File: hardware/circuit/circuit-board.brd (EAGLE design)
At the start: 20 x 73.7 mm, 14 parts, among them U1 ADUM1200CRZ

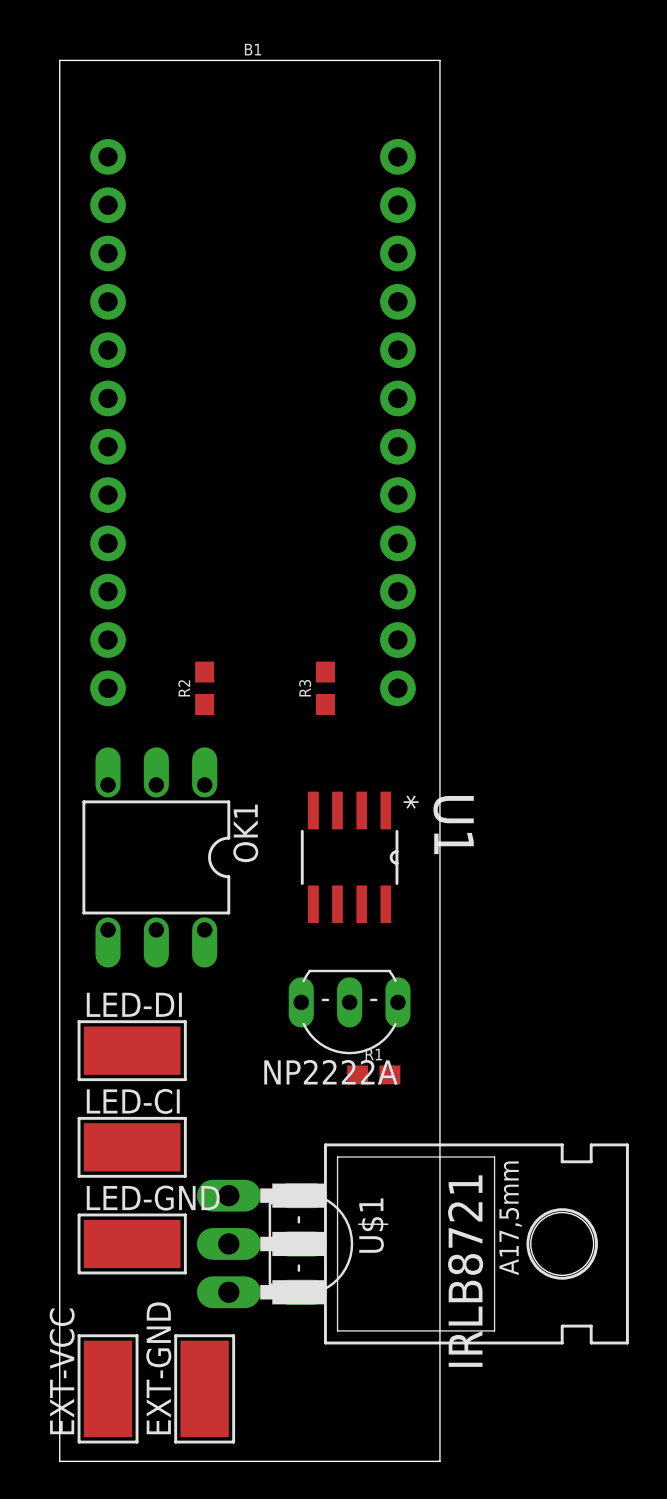
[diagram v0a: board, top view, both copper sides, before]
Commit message: Added autorouted routes, thickened GND-A (LED ground thru MOSFET) traces, this will probably do, will run through DRUs and send it out tomorrow
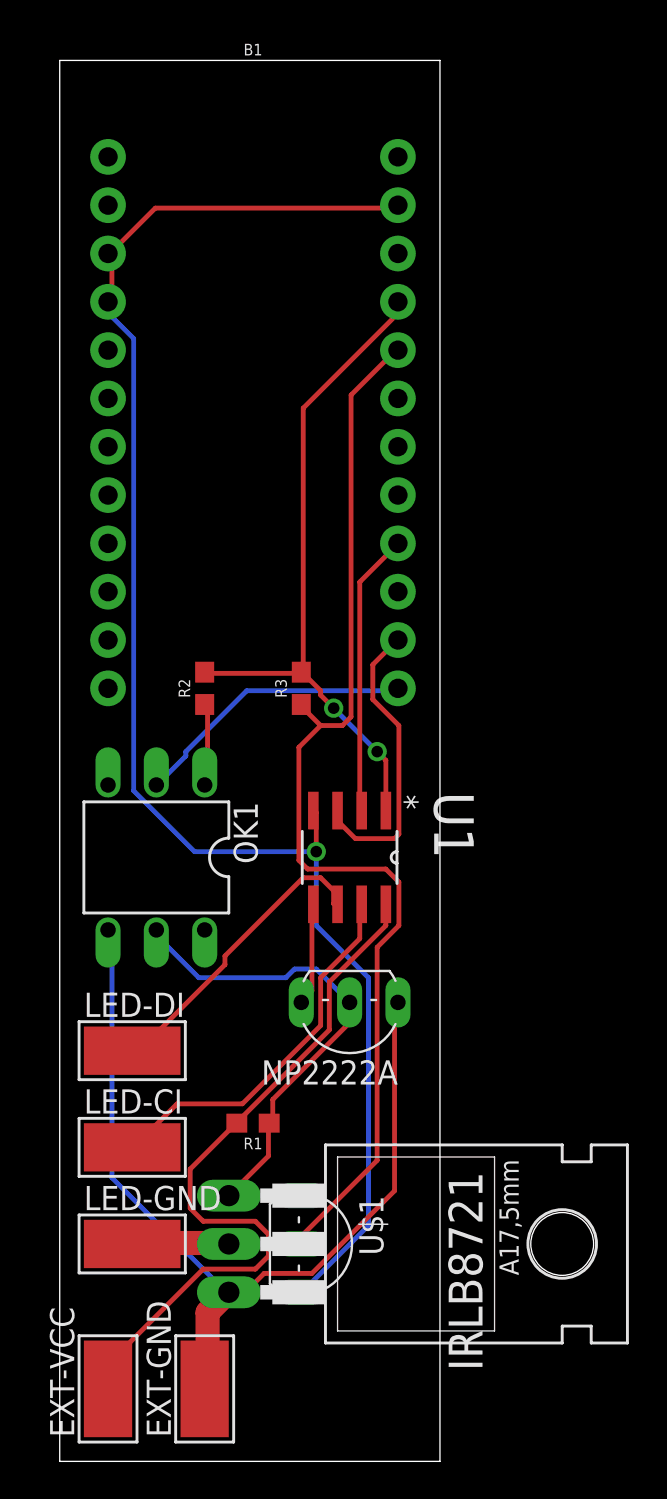
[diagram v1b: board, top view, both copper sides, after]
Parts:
- moved R1 6.84 mm to (10.2, 24.1), turned to 180 degrees
- moved R3 1.27 mm to (12.7, 47.0)
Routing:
- net GND: track 0.00 -> 84.3 mm, vias 0 -> 1
- net TEMP: track 0.00 -> 58.1 mm
- net GNDA: track 0.00 -> 48.5 mm
- net +5V: track 0.00 -> 38.2 mm
- net VCC: track 0.00 -> 35.8 mm, vias 0 -> 2
- net PWR-CTRL: track 0.00 -> 25.2 mm
- net N$7: track 0.00 -> 19.8 mm
- net N$1: track 0.00 -> 15.8 mm
- net N$5: track 0.00 -> 15.6 mm
- net N$8: track 0.00 -> 14.9 mm
- net N$6: track 0.00 -> 14.9 mm
- net ADUM-GND2: track 0.00 -> 5.39 mm
- net N$3: track 0.00 -> 5.10 mm
- net N$4: track 0.00 -> 4.35 mm

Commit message: Added to PCB layout - added ground layers, some labels
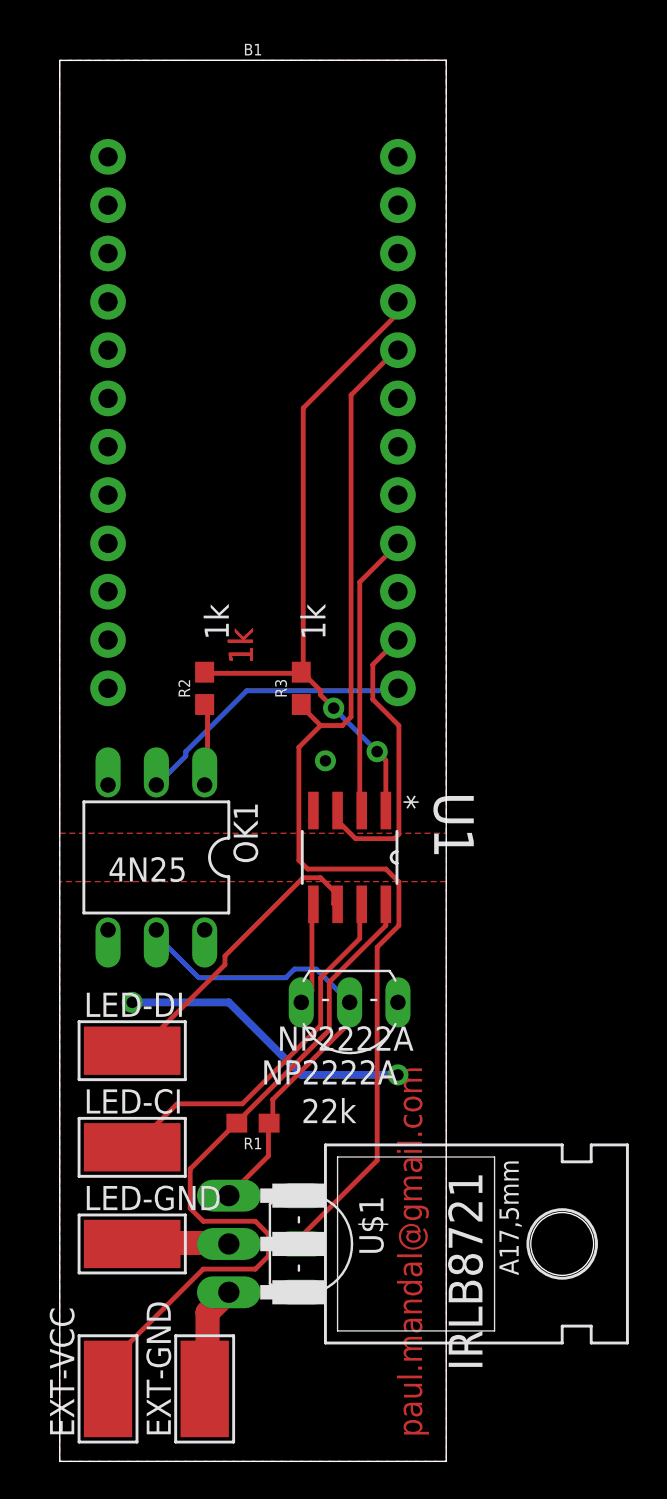
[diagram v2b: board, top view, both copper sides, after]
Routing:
- net GND: track 84.3 -> 0.00 mm
- net GNDA: track 48.5 -> 21.4 mm, vias 0 -> 2
- added copper zone on layer 1, net GND
- added copper zone on layer 16, net GND
- added copper zone on layer 1, net GNDA
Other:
- board size 20 x 73.7 mm -> 20.3 x 73.7 mm
- board text added: "1k"
- board text added: "22k"
- board text added: "4N25"
- board text added: "NP2222A"
- board text added: "paul.mandal@gmail.com"

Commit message: Finished circuit board layout, generating Gerber files now
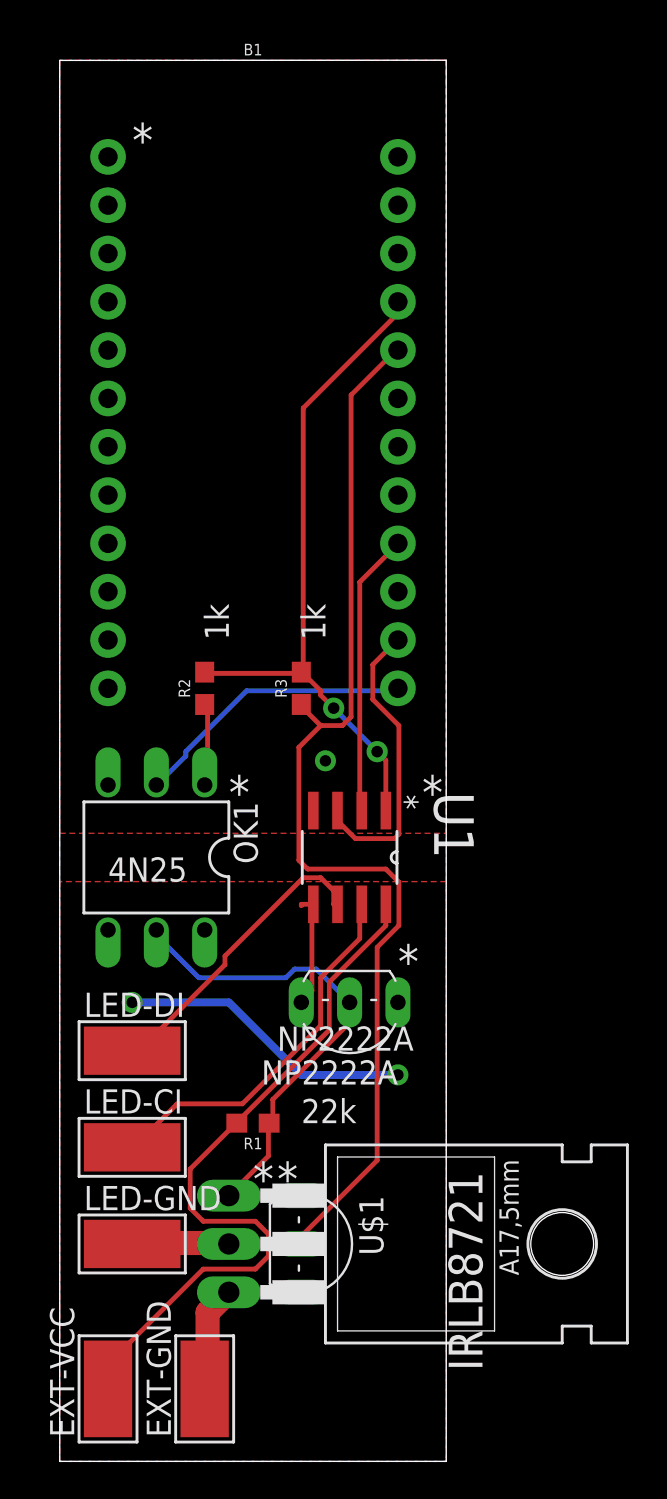
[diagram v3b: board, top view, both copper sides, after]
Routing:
- net ADUM-GND2: track 5.39 -> 6.23 mm
- net VCC: track 35.8 -> 36.4 mm
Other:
- board text added: "*"
- board text removed: "paul.mandal@gmail.com"
